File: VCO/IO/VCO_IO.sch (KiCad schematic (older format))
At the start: 31 parts, among them J1 Saw, J10 Sync, J11 LIN, J12 IO, J2 CV1, J3 CV2, J4 CV3, J5 Pulse, J6 Ramp, J7 Tri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

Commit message: Bunch of bug fixes and tweaks
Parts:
- added H1: Top_MH1, Eurorack:eurorack_mounting_hole, symbol Mechanical:MountingHole_Pad
- added H2: Bottom_MH1, Eurorack:eurorack_mounting_hole, symbol Mechanical:MountingHole_Pad
- added H3: Top_MH2, Eurorack:eurorack_mounting_hole, symbol Mechanical:MountingHole_Pad
- added H4: Bottom_MH2, Eurorack:eurorack_mounting_hole, symbol Mechanical:MountingHole_Pad
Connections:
- net GNDREF: now also H1.1, H2.1, H3.1, H4.1
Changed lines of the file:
@@
 EESchema Schematic File Version 4
-LIBS:AS3340_VCO_IO-cache
-EELAYER 29 0
+LIBS:VCO_IO-cache
+EELAYER 30 0
 EELAYER END
 $Descr A4 11693 8268
@@
 Text Label 9500 4400 0    50   ~ 0
 REAR_CV
+$Comp
+L Mechanical:MountingHole_Pad H1
+U 1 1 5D8EEF13
+P 950 1050
+F 0 "H1" H 1050 1099 50  0000 L CNN
+F 1 "Top_MH1" H 1050 1008 50  0000 L CNN
+F 2 "Eurorack:eurorack_mounting_hole" H 950 1050 50  0001 C CNN
+F 3 "~" H 950 1050 50  0001 C CNN
+	1    950  1050
+	1    0    0    -1
+$EndComp
+$Comp
+L Mechanical:MountingHole_Pad H3
+U 1 1 5D8EF4EF
+P 1550 1050
+F 0 "H3" H 1650 1099 50  0000 L CNN
+F 1 "Top_MH2" H 1650 1008 50  0000 L CNN
+F 2 "Eurorack:eurorack_mounting_hole" H 1550 1050 50  0001 C CNN
+F 3 "~" H 1550 1050 50  0001 C CNN
+	1    1550 1050
+	1    0    0    -1
+$EndComp
+$Comp
+L power:GNDREF #PWR0103
+U 1 1 5D8F337E
+P 950 1150
+F 0 "#PWR0103" H 950 900 50  0001 C CNN
+F 1 "GNDREF" H 955 977 50  0001 C CNN
+F 2 "" H 950 1150 50  0001 C CNN
+F 3 "" H 950 1150 50  0001 C CNN
+	1    950  1150
+	1    0    0    -1
+$EndComp
+$Comp
+L power:GNDREF #PWR0104
+U 1 1 5D8F3BC6
+P 1550 1150
+F 0 "#PWR0104" H 1550 900 50  0001 C CNN
+F 1 "GNDREF" H 1555 977 50  0001 C CNN
+F 2 "" H 1550 1150 50  0001 C CNN
+F 3 "" H 1550 1150 50  0001 C CNN
+	1    1550 1150
+	1    0    0    -1
+$EndComp
+$Comp
+L Mechanical:MountingHole_Pad H2
+U 1 1 5D8F50FF
+P 950 1550
+F 0 "H2" H 1050 1599 50  0000 L CNN
+F 1 "Bottom_MH1" H 1050 1508 50  0000 L CNN
+F 2 "Eurorack:eurorack_mounting_hole" H 950 1550 50  0001 C CNN
+F 3 "~" H 950 1550 50  0001 C CNN
+	1    950  1550
+	1    0    0    -1
+$EndComp
+$Comp
+L Mechanical:MountingHole_Pad H4
+U 1 1 5D8F5105
+P 1550 1550
+F 0 "H4" H 1650 1599 50  0000 L CNN
+F 1 "Bottom_MH2" H 1650 1508 50  0000 L CNN
+F 2 "Eurorack:eurorack_mounting_hole" H 1550 1550 50  0001 C CNN
+F 3 "~" H 1550 1550 50  0001 C CNN
+	1    1550 1550
+	1    0    0    -1
+$EndComp
+$Comp
+L power:GNDREF #PWR0105
+U 1 1 5D8F510B
+P 950 1650
+F 0 "#PWR0105" H 950 1400 50  0001 C CNN
+F 1 "GNDREF" H 955 1477 50  0001 C CNN
+F 2 "" H 950 1650 50  0001 C CNN
+F 3 "" H 950 1650 50  0001 C CNN
+	1    950  1650
+	1    0    0    -1
+$EndComp
+$Comp
+L power:GNDREF #PWR0106
+U 1 1 5D8F5111
+P 1550 1650
+F 0 "#PWR0106" H 1550 1400 50  0001 C CNN
+F 1 "GNDREF" H 1555 1477 50  0001 C CNN
+F 2 "" H 1550 1650 50  0001 C CNN
+F 3 "" H 1550 1650 50  0001 C CNN
+	1    1550 1650
+	1    0    0    -1
+$EndComp
 $EndSCHEMATC

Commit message: Add resistor divider for Sync input and some capacitors.
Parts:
- added C1, C2: C, Capacitor_SMD:C_0805_2012Metric, symbol Device:C
- added R15: 30K, Resistor_SMD:R_0805_2012Metric, symbol Device:R_US
- added R16: 10K, Resistor_SMD:R_0805_2012Metric, symbol Device:R_US
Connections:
- net GNDREF: now also R16.2
- net PWM: now also C2.1
- net SYNC: now also R15.2, R16.1; no longer J10.T
- net at R13.1, R14.2, U1.1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: now also C1.1, C2.2
- net at R11.1, R12.1, R13.2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: now also C1.2
- new net: J10.T, R15.1
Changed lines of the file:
@@
 	1    0    0    -1
 $EndComp
-Wire Wire Line
-	1700 3200 2050 3200
 $Comp
 L Connector:AudioJack2_SwitchT J2
@@
 Text Label 6750 3950 0    50   ~ 0
 CV
-Text Label 2050 3200 0    50   ~ 0
+Text Label 3000 3700 0    50   ~ 0
 SYNC
 Text Label 9500 4300 0    50   ~ 0
@@
 	1    0    0    -1
 $EndComp
+$Comp
+L Device:C C1
+U 1 1 5D96B0F8
+P 5900 3250
+F 0 "C1" V 5648 3250 50  0000 C CNN
+F 1 "C" V 5739 3250 50  0000 C CNN
+F 2 "Capacitor_SMD:C_0805_2012Metric" H 5938 3100 50  0001 C CNN
+F 3 "~" H 5900 3250 50  0001 C CNN
+	1    5900 3250
+	0    1    1    0
+$EndComp
+$Comp
+L Device:C C2
+U 1 1 5D96BB82
+P 6950 3250
+F 0 "C2" V 6698 3250 50  0000 C CNN
+F 1 "C" V 6789 3250 50  0000 C CNN
+F 2 "Capacitor_SMD:C_0805_2012Metric" H 6988 3100 50  0001 C CNN
+F 3 "~" H 6950 3250 50  0001 C CNN
+	1    6950 3250
+	0    1    1    0
+$EndComp
+Wire Wire Line
+	5300 2850 5300 3250
+Wire Wire Line
+	5300 3250 5750 3250
+Connection ~ 5300 2850
+Wire Wire Line
+	6050 3250 6400 3250
+Wire Wire Line
+	6400 3250 6400 2850
+Wire Wire Line
+	6400 3250 6800 3250
+Connection ~ 6400 3250
+Wire Wire Line
+	7400 2850 7400 3250
+Wire Wire Line
+	7400 3250 7100 3250
+Connection ~ 7400 2850
+$Comp
+L Device:R_US R15
+U 1 1 5D97E63C
+P 2600 3450
+F 0 "R15" H 2668 3496 50  0000 L CNN
+F 1 "30K" H 2668 3405 50  0000 L CNN
+F 2 "Resistor_SMD:R_0805_2012Metric" V 2640 3440 50  0001 C CNN
+F 3 "~" H 2600 3450 50  0001 C CNN
+	1    2600 3450
+	1    0    0    -1
+$EndComp
+Wire Wire Line
+	2600 3200 2600 3300
+Wire Wire Line
+	1700 3200 2600 3200
+$Comp
+L Device:R_US R16
+U 1 1 5D9832D3
+P 2600 3950
+F 0 "R16" H 2668 3996 50  0000 L CNN
+F 1 "10K" H 2668 3905 50  0000 L CNN
+F 2 "Resistor_SMD:R_0805_2012Metric" V 2640 3940 50  0001 C CNN
+F 3 "~" H 2600 3950 50  0001 C CNN
+	1    2600 3950
+	1    0    0    -1
+$EndComp
+Wire Wire Line
+	2600 3600 2600 3700
+$Comp
+L power:GNDREF #PWR0107
+U 1 1 5D9880E4
+P 2600 4200
+F 0 "#PWR0107" H 2600 3950 50  0001 C CNN
+F 1 "GNDREF" H 2605 4027 50  0001 C CNN
+F 2 "" H 2600 4200 50  0001 C CNN
+F 3 "" H 2600 4200 50  0001 C CNN
+	1    2600 4200
+	1    0    0    -1
+$EndComp
+Wire Wire Line
+	2600 4200 2600 4100
+Wire Wire Line
+	2600 3700 3000 3700
+Connection ~ 2600 3700
+Wire Wire Line
+	2600 3700 2600 3800
 $EndSCHEMATC

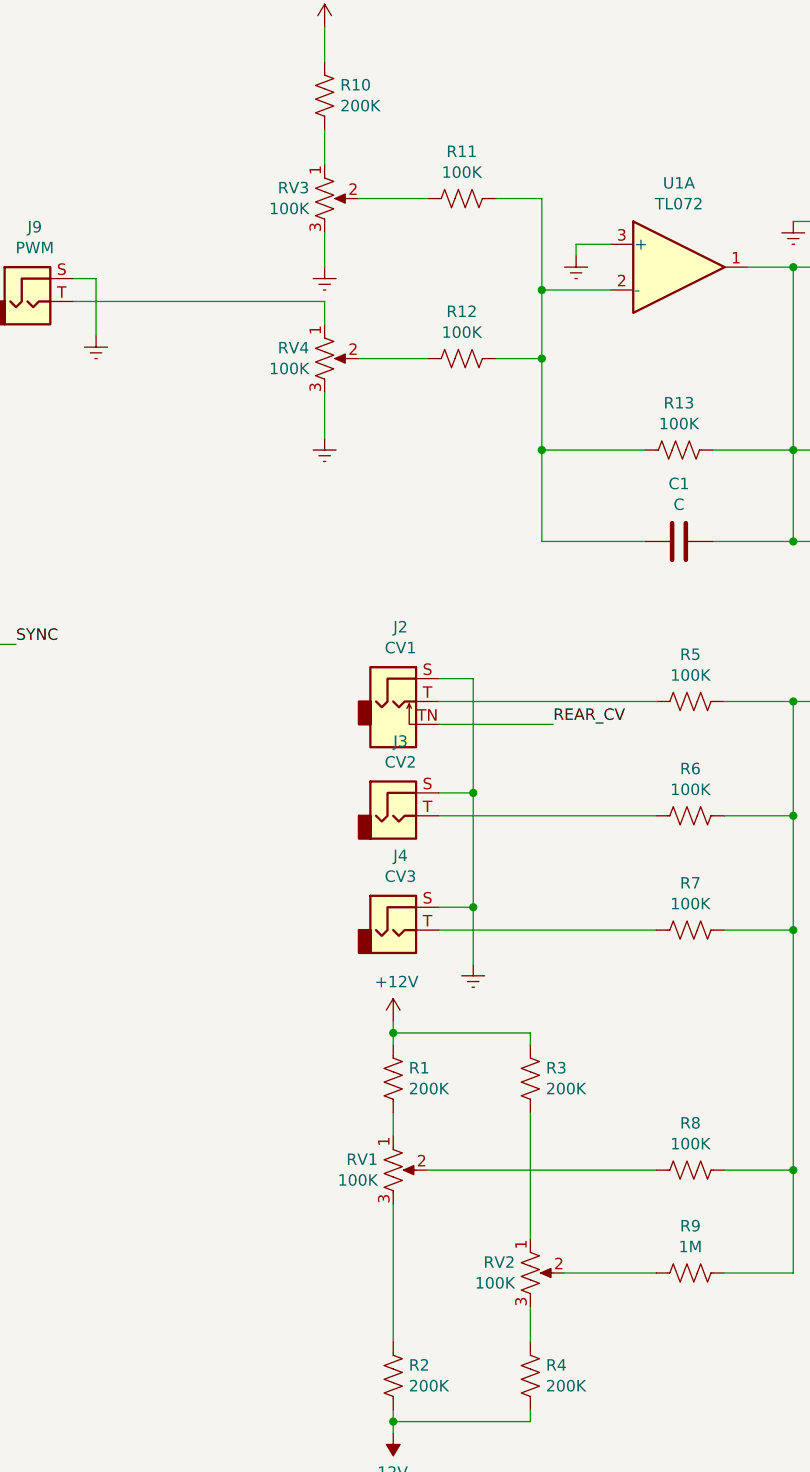
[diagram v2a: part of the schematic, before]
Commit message: Fix backwards knobs
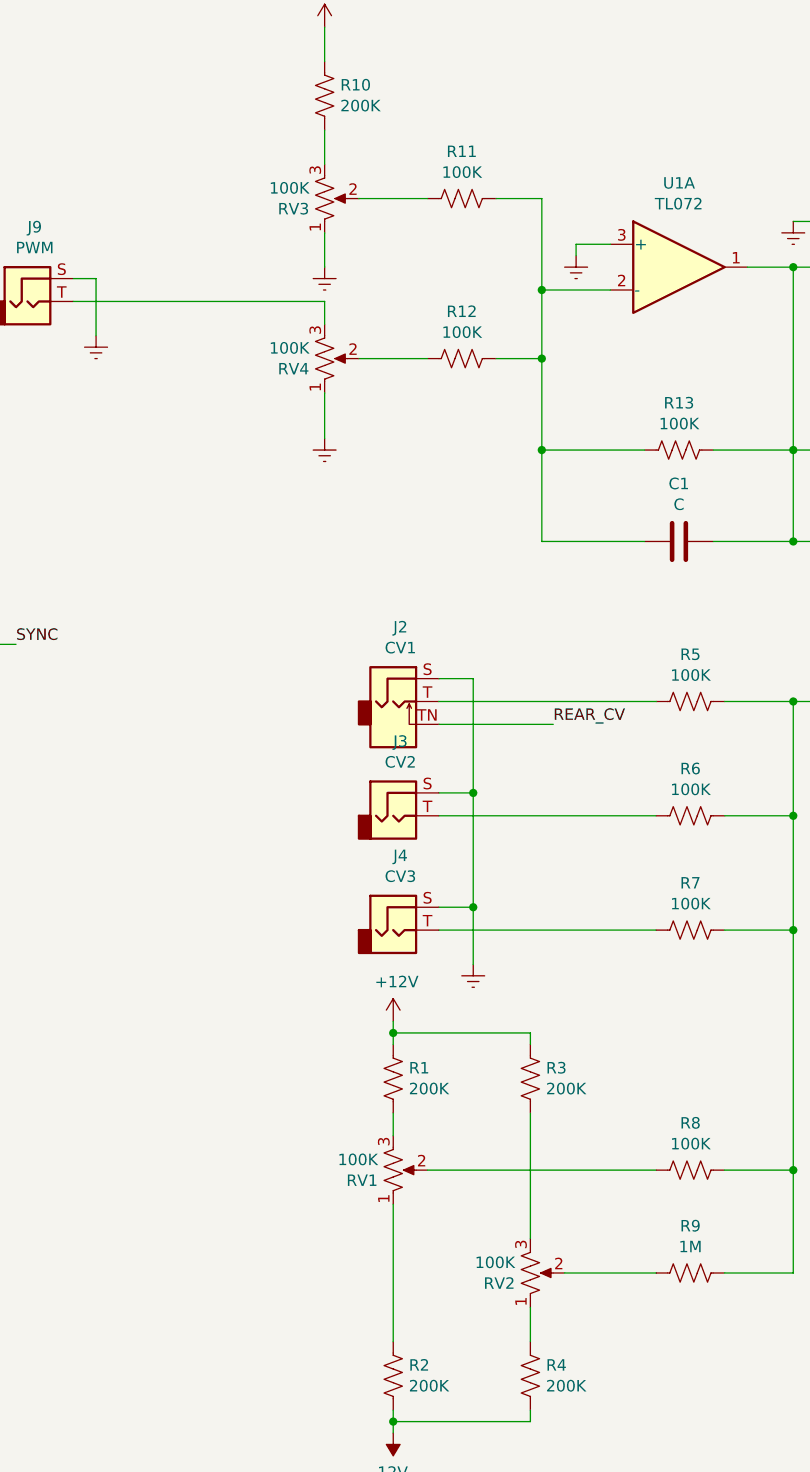
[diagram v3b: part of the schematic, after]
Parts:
- RV1, RV2, RV3, RV4: footprint Eurorack:TT_P0915N -> Eurorack:Potentiometer_TT_P0915N
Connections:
- net GNDREF: now also RV3.1, RV4.1; no longer RV3.3, RV4.3
- net at R10.2: now also RV3.3; no longer RV3.1
- net at J9.T: now also RV4.3; no longer RV4.1
- net at RV2.1: now also R4.1; no longer R3.2
- net at RV2.3: now also R3.2; no longer R4.1
- net at RV1.1: now also R2.1; no longer R1.2
- net at RV1.3: now also R1.2; no longer R2.1
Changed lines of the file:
@@
 F 0 "RV3" H 4283 1796 50  0000 R CNN
 F 1 "100K" H 4283 1705 50  0000 R CNN
-F 2 "Eurorack:TT_P0915N" H 4350 1750 50  0001 C CNN
+F 2 "Eurorack:Potentiometer_TT_P0915N" H 4350 1750 50  0001 C CNN
 F 3 "~" H 4350 1750 50  0001 C CNN
 	1    4350 1750
-	1    0    0    -1
+	1    0    0    1
 $EndComp
 $Comp
@@
 F 0 "RV4" H 4283 2496 50  0000 R CNN
 F 1 "100K" H 4283 2405 50  0000 R CNN
-F 2 "Eurorack:TT_P0915N" H 4350 2450 50  0001 C CNN
+F 2 "Eurorack:Potentiometer_TT_P0915N" H 4350 2450 50  0001 C CNN
 F 3 "~" H 4350 2450 50  0001 C CNN
 	1    4350 2450
-	1    0    0    -1
+	1    0    0    1
 $EndComp
 $Comp
@@
 F 0 "RV2" H 5183 6496 50  0000 R CNN
 F 1 "100K" H 5183 6405 50  0000 R CNN
-F 2 "Eurorack:TT_P0915N" H 5250 6450 50  0001 C CNN
+F 2 "Eurorack:Potentiometer_TT_P0915N" H 5250 6450 50  0001 C CNN
 F 3 "~" H 5250 6450 50  0001 C CNN
 	1    5250 6450
-	1    0    0    -1
+	1    0    0    1
 $EndComp
 $Comp
@@
 F 0 "RV1" H 4583 6046 50  0000 R CNN
 F 1 "100K" H 4583 5955 50  0000 R CNN
-F 2 "Eurorack:TT_P0915N" H 4650 6000 50  0001 C CNN
+F 2 "Eurorack:Potentiometer_TT_P0915N" H 4650 6000 50  0001 C CNN
 F 3 "~" H 4650 6000 50  0001 C CNN
 	1    4650 6000
-	1    0    0    -1
-$EndComp
-$Comp
+	1    0    0    1
+$EndComp
+$Comp
